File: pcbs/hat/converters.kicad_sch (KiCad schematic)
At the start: 16 parts, among them U18 ADS7828, U19 ADS7828, U20 ADS7828, U21 AP2138N-2.5TRG1, U22 LM3480-5.0, U23 SST25VF016B

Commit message: beginning of the layout
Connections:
- net SENSOR_10: now also U18.8 (CH7); no longer U18.1 (CH0)
- net SENSOR_11: now also U19.8 (CH7); no longer U19.1 (CH0)
- net SENSOR_12: now also U20.8 (CH7); no longer U20.1 (CH0)
- net SENSOR_20: now also U18.7 (CH6); no longer U18.2 (CH1)
- net SENSOR_21: now also U19.7 (CH6); no longer U19.2 (CH1)
- net SENSOR_22: now also U20.7 (CH6); no longer U20.2 (CH1)
- net SENSOR_30: now also U18.6 (CH5); no longer U18.3 (CH2)
- net SENSOR_31: now also U19.6 (CH5); no longer U19.3 (CH2)
- net SENSOR_32: now also U20.6 (CH5); no longer U20.3 (CH2)
- net SENSOR_40: now also U18.5 (CH4); no longer U18.4 (CH3)
- net SENSOR_41: now also U19.5 (CH4); no longer U19.4 (CH3)
- net SENSOR_42: now also U20.5 (CH4); no longer U20.4 (CH3)
- net SENSOR_50: now also U18.4 (CH3); no longer U18.5 (CH4)
- net SENSOR_51: now also U19.4 (CH3); no longer U19.5 (CH4)
- net SENSOR_52: now also U20.4 (CH3); no longer U20.5 (CH4)
- net SENSOR_60: now also U18.3 (CH2); no longer U18.6 (CH5)
- net SENSOR_61: now also U19.3 (CH2); no longer U19.6 (CH5)
- net SENSOR_62: now also U20.3 (CH2); no longer U20.6 (CH5)
- net SENSOR_70: now also U18.2 (CH1); no longer U18.7 (CH6)
- net SENSOR_71: now also U19.2 (CH1); no longer U19.7 (CH6)
- net SENSOR_72: now also U20.2 (CH1); no longer U20.7 (CH6)
- net SENSOR_80: now also U18.1 (CH0); no longer U18.8 (CH7)
- net SENSOR_81: now also U19.1 (CH0); no longer U19.8 (CH7)
- net SENSOR_82: now also U20.1 (CH0); no longer U20.8 (CH7)
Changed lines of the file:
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@@
     (effects (font (size 1.27 1.27)) (justify left bottom))
   )
-  (label "SENSOR_62" (at 46.99 168.275 0)
+  (label "SENSOR_62" (at 47.625 160.655 0)
     (effects (font (size 1.27 1.27)) (justify left bottom))
   )
-  (label "SENSOR_12" (at 46.99 155.575 0)
+  (label "SENSOR_12" (at 47.625 173.355 0)
     (effects (font (size 1.27 1.27)) (justify left bottom))
   )
-  (label "SENSOR_40" (at 46.99 55.245 0)
+  (label "SENSOR_40" (at 47.625 57.785 0)
     (effects (font (size 1.27 1.27)) (justify left bottom))
   )
-  (label "SENSOR_21" (at 46.99 104.14 0)
+  (label "SENSOR_21" (at 47.625 116.84 0)
     (effects (font (size 1.27 1.27)) (justify left bottom))
   )
-  (label "SENSOR_20" (at 46.99 50.165 0)
+  (label "SENSOR_20" (at 47.625 62.865 0)
     (effects (font (size 1.27 1.27)) (justify left bottom))
   )
-  (label "SENSOR_50" (at 46.99 57.785 0)
+  (label "SENSOR_50" (at 47.625 55.245 0)
     (effects (font (size 1.27 1.27)) (justify left bottom))
   )
-  (label "SENSOR_31" (at 46.99 106.68 0)
+  (label "SENSOR_31" (at 47.625 114.3 0)
     (effects (font (size 1.27 1.27)) (justify left bottom))
   )
-  (label "SENSOR_52" (at 46.99 165.735 0)
+  (label "SENSOR_52" (at 47.625 163.195 0)
     (effects (font (size 1.27 1.27)) (justify left bottom))
   )
-  (label "SENSOR_51" (at 46.99 111.76 0)
+  (label "SENSOR_51" (at 47.625 109.22 0)
     (effects (font (size 1.27 1.27)) (justify left bottom))
   )
-  (label "SENSOR_80" (at 46.99 65.405 0)
+  (label "SENSOR_80" (at 47.625 47.625 0)
     (effects (font (size 1.27 1.27)) (justify left bottom))
   )
-  (label "SENSOR_81" (at 46.99 119.38 0)
+  (label "SENSOR_81" (at 47.625 101.6 0)
     (effects (font (size 1.27 1.27)) (justify left bottom))
   )
-  (label "SENSOR_72" (at 46.99 170.815 0)
+  (label "SENSOR_72" (at 47.625 158.115 0)
     (effects (font (size 1.27 1.27)) (justify left bottom))
   )
-  (label "SENSOR_60" (at 46.99 60.325 0)
+  (label "SENSOR_60" (at 47.625 52.705 0)
     (effects (font (size 1.27 1.27)) (justify left bottom))
   )
-  (label "SENSOR_41" (at 46.99 109.22 0)
+  (label "SENSOR_41" (at 47.625 111.76 0)
     (effects (font (size 1.27 1.27)) (justify left bottom))
   )
@@
     (effects (font (size 1.27 1.27)) (justify right bottom))
   )
-  (label "SENSOR_32" (at 46.99 160.655 0)
+  (label "SENSOR_32" (at 47.625 168.275 0)
     (effects (font (size 1.27 1.27)) (justify left bottom))
   )
@@
     (effects (font (size 1.27 1.27)) (justify right bottom))
   )
-  (label "SENSOR_11" (at 46.99 101.6 0)
+  (label "SENSOR_11" (at 47.625 119.38 0)
     (effects (font (size 1.27 1.27)) (justify left bottom))
   )
-  (label "SENSOR_30" (at 46.99 52.705 0)
+  (label "SENSOR_30" (at 47.625 60.325 0)
     (effects (font (size 1.27 1.27)) (justify left bottom))
   )
-  (label "SENSOR_10" (at 46.99 47.625 0)
+  (label "SENSOR_10" (at 47.625 65.405 0)
     (effects (font (size 1.27 1.27)) (justify left bottom))
   )
-  (label "SENSOR_82" (at 46.99 173.355 0)
+  (label "SENSOR_82" (at 47.625 155.575 0)
     (effects (font (size 1.27 1.27)) (justify left bottom))
   )
-  (label "SENSOR_71" (at 46.99 116.84 0)
+  (label "SENSOR_71" (at 47.625 104.14 0)
     (effects (font (size 1.27 1.27)) (justify left bottom))
   )
-  (label "SENSOR_61" (at 46.99 114.3 0)
+  (label "SENSOR_61" (at 47.625 106.68 0)
     (effects (font (size 1.27 1.27)) (justify left bottom))
   )
-  (label "SENSOR_22" (at 46.99 158.115 0)
+  (label "SENSOR_22" (at 47.625 170.815 0)
     (effects (font (size 1.27 1.27)) (justify left bottom))
   )
@@
     (effects (font (size 1.27 1.27)) (justify right bottom))
   )
-  (label "SENSOR_42" (at 46.99 163.195 0)
+  (label "SENSOR_42" (at 47.625 165.735 0)
     (effects (font (size 1.27 1.27)) (justify left bottom))
   )
-  (label "SENSOR_70" (at 46.99 62.865 0)
+  (label "SENSOR_70" (at 47.625 50.165 0)
     (effects (font (size 1.27 1.27)) (justify left bottom))
   )

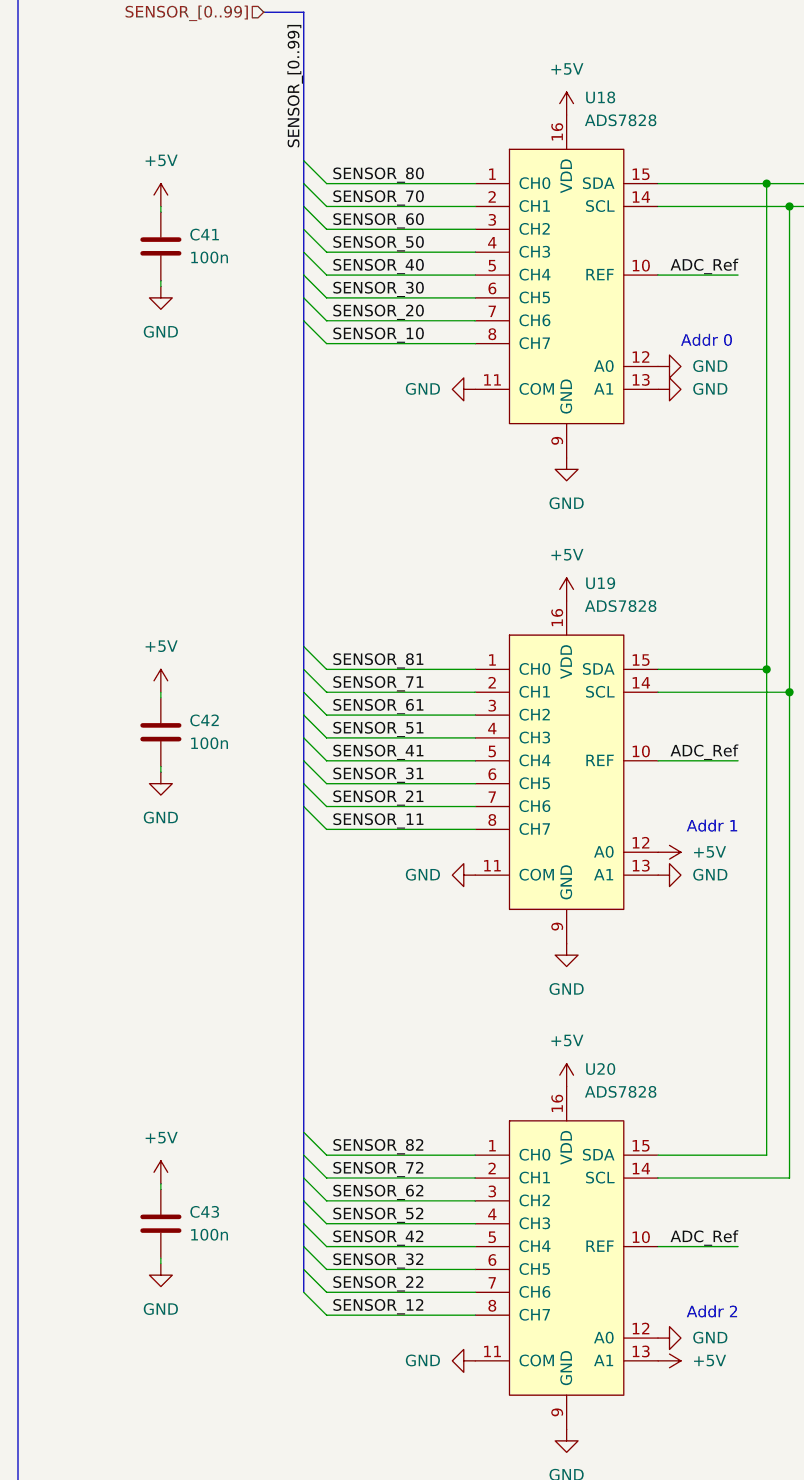
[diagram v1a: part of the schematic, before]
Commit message: reassign adc's
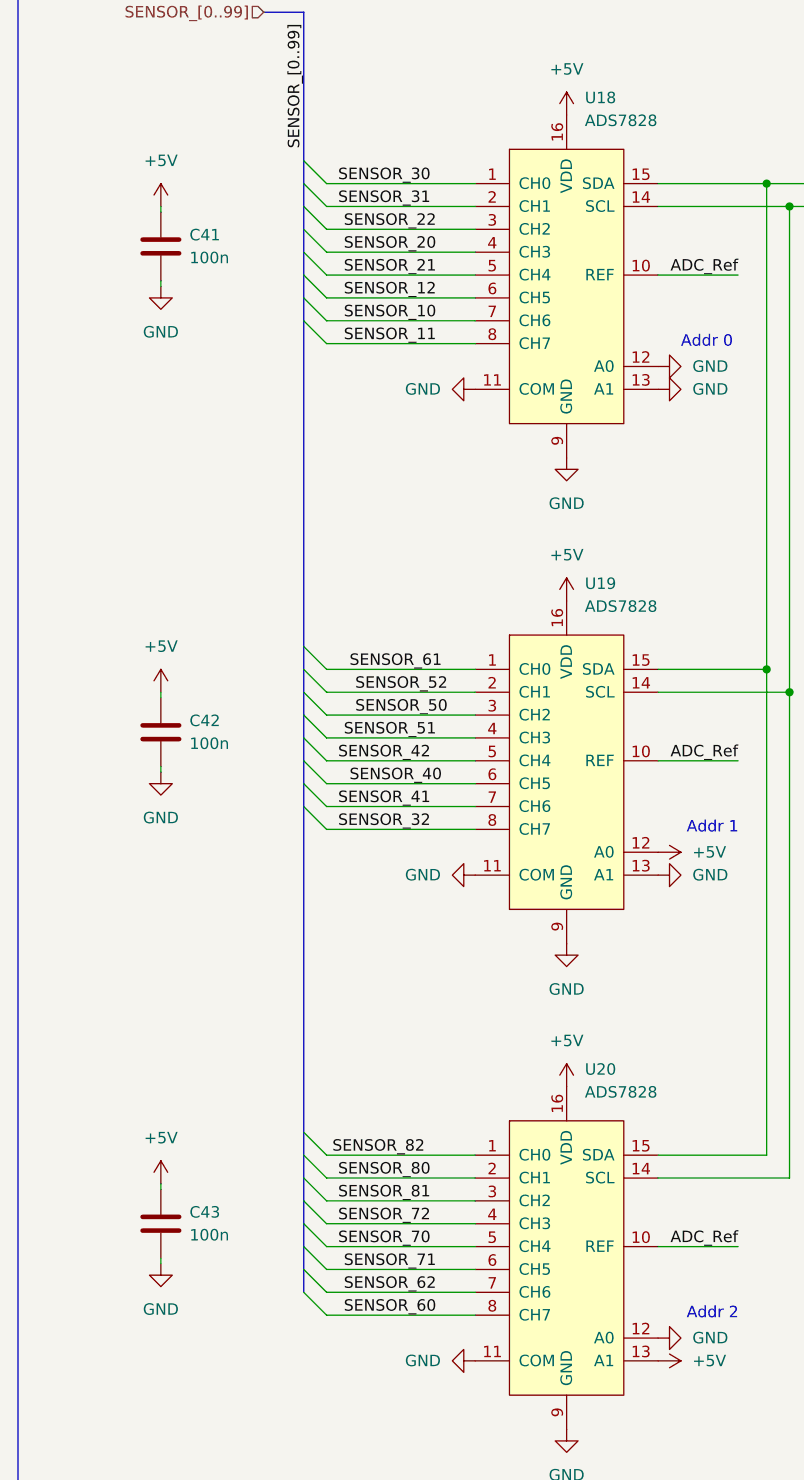
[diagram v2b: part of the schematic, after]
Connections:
- net SENSOR_10: now also U18.7 (CH6); no longer U18.8 (CH7)
- net SENSOR_11: now also U18.8 (CH7); no longer U19.8 (CH7)
- net SENSOR_12: now also U18.6 (CH5); no longer U20.8 (CH7)
- net SENSOR_20: now also U18.4 (CH3); no longer U18.7 (CH6)
- net SENSOR_21: now also U18.5 (CH4); no longer U19.7 (CH6)
- net SENSOR_22: now also U18.3 (CH2); no longer U20.7 (CH6)
- net SENSOR_30: now also U18.1 (CH0); no longer U18.6 (CH5)
- net SENSOR_31: now also U18.2 (CH1); no longer U19.6 (CH5)
- net SENSOR_32: now also U19.8 (CH7); no longer U20.6 (CH5)
- net SENSOR_40: now also U19.6 (CH5); no longer U18.5 (CH4)
- net SENSOR_41: now also U19.7 (CH6); no longer U19.5 (CH4)
- net SENSOR_42: now also U19.5 (CH4); no longer U20.5 (CH4)
- net SENSOR_50: now also U19.3 (CH2); no longer U18.4 (CH3)
- net SENSOR_52: now also U19.2 (CH1); no longer U20.4 (CH3)
- net SENSOR_60: now also U20.8 (CH7); no longer U18.3 (CH2)
- net SENSOR_61: now also U19.1 (CH0); no longer U19.3 (CH2)
- net SENSOR_62: now also U20.7 (CH6); no longer U20.3 (CH2)
- net SENSOR_70: now also U20.5 (CH4); no longer U18.2 (CH1)
- net SENSOR_71: now also U20.6 (CH5); no longer U19.2 (CH1)
- net SENSOR_72: now also U20.4 (CH3); no longer U20.2 (CH1)
- net SENSOR_80: now also U20.2 (CH1); no longer U18.1 (CH0)
- net SENSOR_81: now also U20.3 (CH2); no longer U19.1 (CH0)
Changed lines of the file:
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@@
     (effects (font (size 1.27 1.27)) (justify left bottom))
   )
-  (label "SENSOR_62" (at 47.625 160.655 0)
+  (label "SENSOR_62" (at 48.895 170.815 0)
     (effects (font (size 1.27 1.27)) (justify left bottom))
   )
-  (label "SENSOR_12" (at 47.625 173.355 0)
+  (label "SENSOR_12" (at 48.895 60.325 0)
     (effects (font (size 1.27 1.27)) (justify left bottom))
   )
-  (label "SENSOR_40" (at 47.625 57.785 0)
+  (label "SENSOR_40" (at 49.53 114.3 0)
     (effects (font (size 1.27 1.27)) (justify left bottom))
   )
-  (label "SENSOR_21" (at 47.625 116.84 0)
+  (label "SENSOR_21" (at 48.895 57.785 0)
     (effects (font (size 1.27 1.27)) (justify left bottom))
   )
-  (label "SENSOR_20" (at 47.625 62.865 0)
+  (label "SENSOR_20" (at 48.895 55.245 0)
     (effects (font (size 1.27 1.27)) (justify left bottom))
   )
-  (label "SENSOR_50" (at 47.625 55.245 0)
+  (label "SENSOR_50" (at 50.165 106.68 0)
     (effects (font (size 1.27 1.27)) (justify left bottom))
   )
-  (label "SENSOR_31" (at 47.625 114.3 0)
+  (label "SENSOR_31" (at 48.26 50.165 0)
     (effects (font (size 1.27 1.27)) (justify left bottom))
   )
-  (label "SENSOR_52" (at 47.625 163.195 0)
+  (label "SENSOR_52" (at 50.165 104.14 0)
     (effects (font (size 1.27 1.27)) (justify left bottom))
   )
-  (label "SENSOR_51" (at 47.625 109.22 0)
+  (label "SENSOR_51" (at 48.895 109.22 0)
     (effects (font (size 1.27 1.27)) (justify left bottom))
   )
-  (label "SENSOR_80" (at 47.625 47.625 0)
+  (label "SENSOR_80" (at 48.26 158.115 0)
     (effects (font (size 1.27 1.27)) (justify left bottom))
   )
-  (label "SENSOR_81" (at 47.625 101.6 0)
+  (label "SENSOR_81" (at 48.26 160.655 0)
     (effects (font (size 1.27 1.27)) (justify left bottom))
   )
-  (label "SENSOR_72" (at 47.625 158.115 0)
+  (label "SENSOR_72" (at 48.26 163.195 0)
     (effects (font (size 1.27 1.27)) (justify left bottom))
   )
-  (label "SENSOR_60" (at 47.625 52.705 0)
+  (label "SENSOR_60" (at 48.895 173.355 0)
     (effects (font (size 1.27 1.27)) (justify left bottom))
   )
-  (label "SENSOR_41" (at 47.625 111.76 0)
+  (label "SENSOR_41" (at 48.26 116.84 0)
     (effects (font (size 1.27 1.27)) (justify left bottom))
   )
@@
     (effects (font (size 1.27 1.27)) (justify right bottom))
   )
-  (label "SENSOR_32" (at 47.625 168.275 0)
+  (label "SENSOR_32" (at 48.26 119.38 0)
     (effects (font (size 1.27 1.27)) (justify left bottom))
   )
@@
     (effects (font (size 1.27 1.27)) (justify right bottom))
   )
-  (label "SENSOR_11" (at 47.625 119.38 0)
+  (label "SENSOR_11" (at 48.895 65.405 0)
     (effects (font (size 1.27 1.27)) (justify left bottom))
   )
-  (label "SENSOR_30" (at 47.625 60.325 0)
+  (label "SENSOR_30" (at 48.26 47.625 0)
     (effects (font (size 1.27 1.27)) (justify left bottom))
   )
-  (label "SENSOR_10" (at 47.625 65.405 0)
+  (label "SENSOR_10" (at 48.895 62.865 0)
     (effects (font (size 1.27 1.27)) (justify left bottom))
   )
@@
     (effects (font (size 1.27 1.27)) (justify left bottom))
   )
-  (label "SENSOR_71" (at 47.625 104.14 0)
+  (label "SENSOR_71" (at 48.895 168.275 0)
     (effects (font (size 1.27 1.27)) (justify left bottom))
   )
-  (label "SENSOR_61" (at 47.625 106.68 0)
+  (label "SENSOR_61" (at 49.53 101.6 0)
     (effects (font (size 1.27 1.27)) (justify left bottom))
   )
-  (label "SENSOR_22" (at 47.625 170.815 0)
+  (label "SENSOR_22" (at 48.895 52.705 0)
     (effects (font (size 1.27 1.27)) (justify left bottom))
   )
@@
     (effects (font (size 1.27 1.27)) (justify right bottom))
   )
-  (label "SENSOR_42" (at 47.625 165.735 0)
+  (label "SENSOR_42" (at 48.26 111.76 0)
     (effects (font (size 1.27 1.27)) (justify left bottom))
   )
-  (label "SENSOR_70" (at 47.625 50.165 0)
+  (label "SENSOR_70" (at 48.26 165.735 0)
     (effects (font (size 1.27 1.27)) (justify left bottom))
   )
@@
   )
   (symbol (lib_id "power:GND") (at 63.5 70.485 270) (unit 1)
-    (in_bom yes) (on_board yes) (fields_autoplaced)
+    (in_bom yes) (on_board yes)
     (property "Reference" "#PWR0133" (id 0) (at 57.15 70.485 0)
       (effects (font (size 1.27 1.27)) hide)

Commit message: pcb layout progress
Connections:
- net SENSOR_12: now also U18.5 (CH4); no longer U18.6 (CH5)
- net SENSOR_21: now also U18.6 (CH5); no longer U18.5 (CH4)
- net SENSOR_22: now also U18.2 (CH1); no longer U18.3 (CH2)
- net SENSOR_31: now also U18.3 (CH2); no longer U18.2 (CH1)
- net SENSOR_32: now also U19.7 (CH6); no longer U19.8 (CH7)
- net SENSOR_41: now also U19.8 (CH7); no longer U19.7 (CH6)
- net SENSOR_52: now also U19.1 (CH0); no longer U19.2 (CH1)
- net SENSOR_61: now also U19.2 (CH1); no longer U19.1 (CH0)
- net SENSOR_62: now also U20.6 (CH5); no longer U20.7 (CH6)
- net SENSOR_71: now also U20.7 (CH6); no longer U20.6 (CH5)
- net SENSOR_72: now also U20.3 (CH2); no longer U20.4 (CH3)
- net SENSOR_81: now also U20.4 (CH3); no longer U20.3 (CH2)
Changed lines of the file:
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@@
     (effects (font (size 1.27 1.27)) (justify left bottom))
   )
-  (label "SENSOR_62" (at 48.895 170.815 0)
+  (label "SENSOR_62" (at 48.26 168.275 0)
     (effects (font (size 1.27 1.27)) (justify left bottom))
   )
-  (label "SENSOR_12" (at 48.895 60.325 0)
+  (label "SENSOR_12" (at 49.53 57.785 0)
     (effects (font (size 1.27 1.27)) (justify left bottom))
   )
@@
     (effects (font (size 1.27 1.27)) (justify left bottom))
   )
-  (label "SENSOR_21" (at 48.895 57.785 0)
+  (label "SENSOR_21" (at 49.53 60.325 0)
     (effects (font (size 1.27 1.27)) (justify left bottom))
   )
@@
     (effects (font (size 1.27 1.27)) (justify left bottom))
   )
-  (label "SENSOR_31" (at 48.26 50.165 0)
+  (label "SENSOR_31" (at 48.895 52.705 0)
     (effects (font (size 1.27 1.27)) (justify left bottom))
   )
-  (label "SENSOR_52" (at 50.165 104.14 0)
+  (label "SENSOR_52" (at 50.165 101.6 0)
     (effects (font (size 1.27 1.27)) (justify left bottom))
   )
@@
     (effects (font (size 1.27 1.27)) (justify left bottom))
   )
-  (label "SENSOR_81" (at 48.26 160.655 0)
+  (label "SENSOR_81" (at 48.895 163.195 0)
     (effects (font (size 1.27 1.27)) (justify left bottom))
   )
-  (label "SENSOR_72" (at 48.26 163.195 0)
+  (label "SENSOR_72" (at 47.625 160.655 0)
     (effects (font (size 1.27 1.27)) (justify left bottom))
   )
@@
     (effects (font (size 1.27 1.27)) (justify left bottom))
   )
-  (label "SENSOR_41" (at 48.26 116.84 0)
+  (label "SENSOR_41" (at 48.26 119.38 0)
     (effects (font (size 1.27 1.27)) (justify left bottom))
   )
@@
     (effects (font (size 1.27 1.27)) (justify right bottom))
   )
-  (label "SENSOR_32" (at 48.26 119.38 0)
+  (label "SENSOR_32" (at 48.26 116.84 0)
     (effects (font (size 1.27 1.27)) (justify left bottom))
   )
@@
     (effects (font (size 1.27 1.27)) (justify left bottom))
   )
-  (label "SENSOR_71" (at 48.895 168.275 0)
+  (label "SENSOR_71" (at 49.53 170.815 0)
     (effects (font (size 1.27 1.27)) (justify left bottom))
   )
-  (label "SENSOR_61" (at 49.53 101.6 0)
+  (label "SENSOR_61" (at 50.165 104.14 0)
     (effects (font (size 1.27 1.27)) (justify left bottom))
   )
-  (label "SENSOR_22" (at 48.895 52.705 0)
+  (label "SENSOR_22" (at 49.53 50.165 0)
     (effects (font (size 1.27 1.27)) (justify left bottom))
   )
@@
     (effects (font (size 1.27 1.27)) (justify right bottom))
   )
-  (label "SENSOR_42" (at 48.26 111.76 0)
+  (label "SENSOR_42" (at 48.895 111.76 0)
     (effects (font (size 1.27 1.27)) (justify left bottom))
   )
